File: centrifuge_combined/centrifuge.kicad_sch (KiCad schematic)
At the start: 4 parts, among them J504 Conn_02x05_Odd_Even, J518 Conn_02x03_Odd_Even, J519 Conn_02x02_Odd_Even

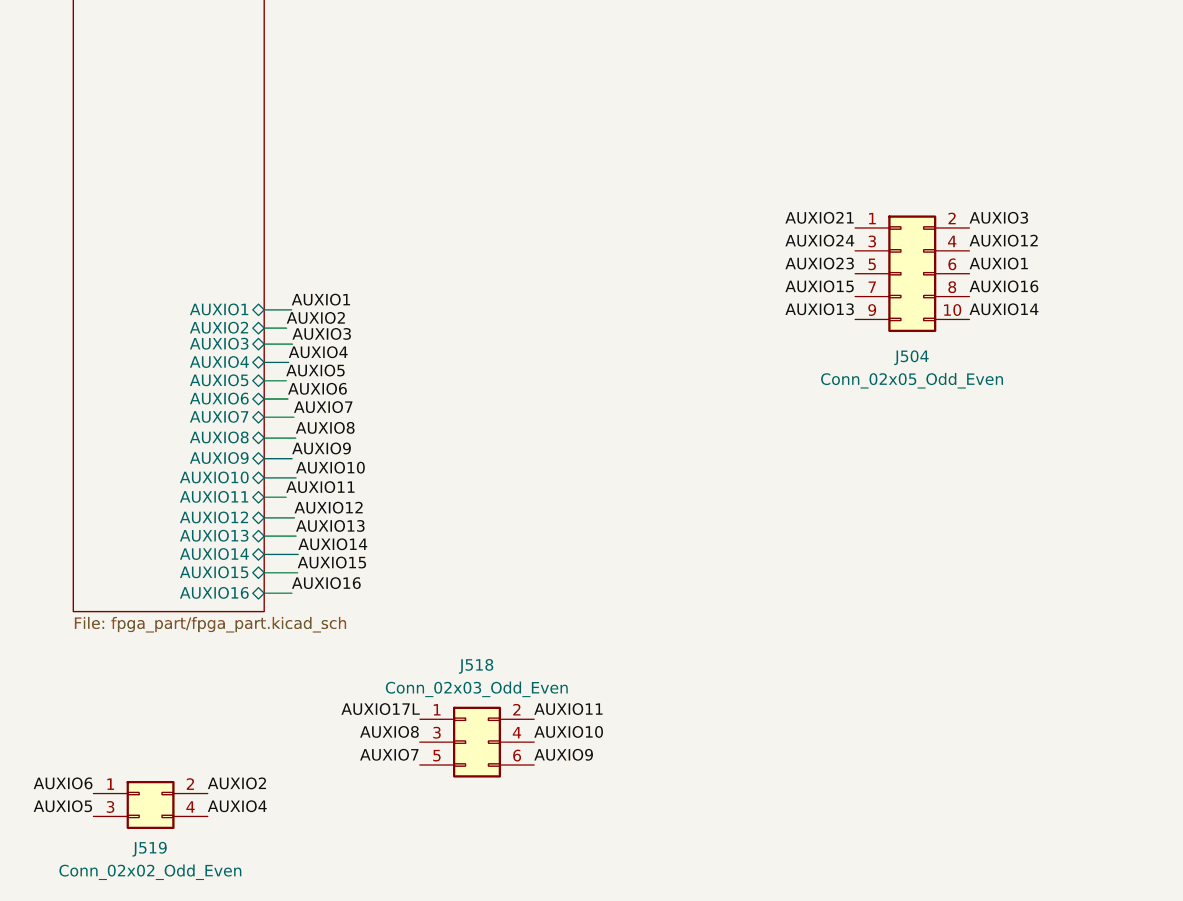
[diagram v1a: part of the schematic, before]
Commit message: more checks, also make silkscreen text for connectors
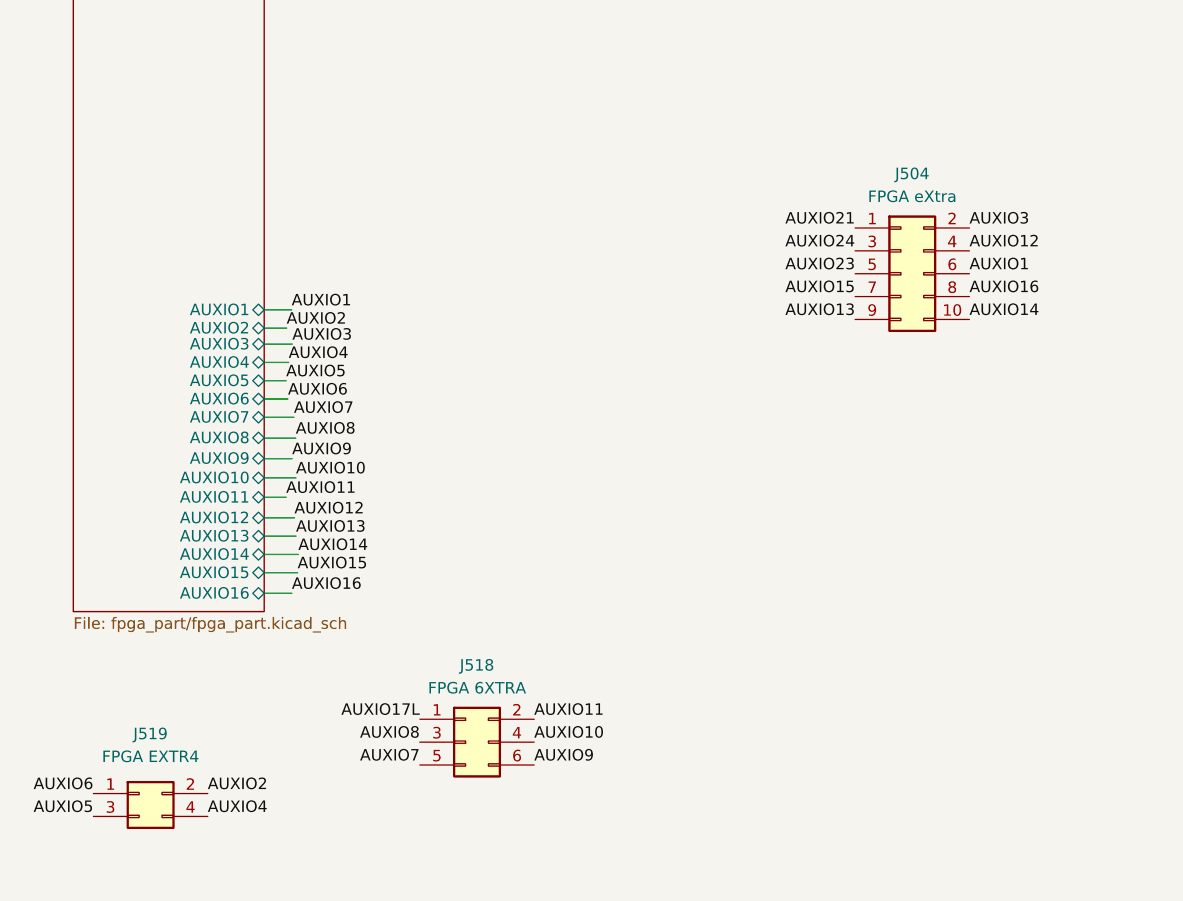
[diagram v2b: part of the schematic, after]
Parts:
- J504: value Conn_02x05_Odd_Even -> FPGA eXtra
- J518: value Conn_02x03_Odd_Even -> FPGA 6XTRA
- J519: value Conn_02x02_Odd_Even -> FPGA EXTR4
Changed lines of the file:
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@@
     (in_bom yes) (on_board yes) (fields_autoplaced)
     (property "Reference" "J518" (id 0) (at 114.1984 172.72 0))
-    (property "Value" "Conn_02x03_Odd_Even" (id 1) (at 114.1984 175.26 0))
+    (property "Value" "FPGA 6XTRA" (id 1) (at 114.1984 175.26 0))
     (property "Footprint" "Connector_PinHeader_2.54mm:PinHeader_2x03_P2.54mm_Vertical" (id 2) (at 112.9284 181.2544 0)
       (effects (font (size 1.27 1.27)) hide)
@@
   (symbol (lib_id "Connector_Generic:Conn_02x02_Odd_Even") (at 76.6572 186.9694 0) (unit 1)
     (in_bom yes) (on_board yes) (fields_autoplaced)
-    (property "Reference" "J519" (id 0) (at 77.9272 193.04 0))
-    (property "Value" "Conn_02x02_Odd_Even" (id 1) (at 77.9272 195.58 0))
+    (property "Reference" "J519" (id 0) (at 77.9272 180.34 0))
+    (property "Value" "FPGA EXTR4" (id 1) (at 77.9272 182.88 0))
     (property "Footprint" "Connector_PinHeader_2.54mm:PinHeader_2x02_P2.54mm_Vertical" (id 2) (at 76.6572 186.9694 0)
       (effects (font (size 1.27 1.27)) hide)
@@
   (symbol (lib_id "Connector_Generic:Conn_02x05_Odd_Even") (at 161.29 129.2098 0) (unit 1)
     (in_bom yes) (on_board yes) (fields_autoplaced)
-    (property "Reference" "J504" (id 0) (at 162.56 138.43 0))
-    (property "Value" "Conn_02x05_Odd_Even" (id 1) (at 162.56 140.97 0))
+    (property "Reference" "J504" (id 0) (at 162.56 118.11 0))
+    (property "Value" "FPGA eXtra" (id 1) (at 162.56 120.65 0))
     (property "Footprint" "Connector_PinHeader_2.54mm:PinHeader_2x05_P2.54mm_Vertical" (id 2) (at 161.29 129.2098 0)
       (effects (font (size 1.27 1.27)) hide)
@@
       (reference "#PWR0122") (unit 1) (value "+5V") (footprint "")
     )
+    (path "/e1575795-d3d5-4c3d-a0f9-e66719ec181c/98fec552-a155-4b2e-a0db-8f682b2e047b"
+      (reference "#PWR0123") (unit 1) (value "+3V3_FPGA") (footprint "")
+    )
     (path "/e1575795-d3d5-4c3d-a0f9-e66719ec181c/9c253e80-2b56-46fb-bbe0-8c25e23a6733/cee8dd18-ae90-4ef7-82e5-f924274ba04a"
       (reference "#PWR0124") (unit 1) (value "+3V3") (footprint "")
@@
       (reference "#PWR0189") (unit 1) (value "+5V_FPGA") (footprint "")
     )
+    (path "/e1575795-d3d5-4c3d-a0f9-e66719ec181c/f1e8b8ff-8293-4a66-bf3d-2505ef83bc55"
+      (reference "#PWR0190") (unit 1) (value "+3V3_FPGA") (footprint "")
+    )
     (path "/e1575795-d3d5-4c3d-a0f9-e66719ec181c/41448e64-f8a6-4898-94db-9af1b3d7cee9/dd33a722-3105-430e-ae1f-18734fe91dc7"
       (reference "#PWR0191") (unit 1) (value "GND") (footprint "")
@@
       (reference "#PWR0539") (unit 1) (value "GND") (footprint "")
     )
-    (path "/e1575795-d3d5-4c3d-a0f9-e66719ec181c/98fec552-a155-4b2e-a0db-8f682b2e047b"
-      (reference "#PWR?") (unit 1) (value "+3V3_FPGA") (footprint "")
-    )
-    (path "/e1575795-d3d5-4c3d-a0f9-e66719ec181c/f1e8b8ff-8293-4a66-bf3d-2505ef83bc55"
-      (reference "#PWR?") (unit 1) (value "+3V3_FPGA") (footprint "")
-    )
     (path "/e1575795-d3d5-4c3d-a0f9-e66719ec181c/634c7769-4266-4d3f-b715-4b9767b6d9de/90142074-d6ae-4f09-8dd2-e143c0d83720"
       (reference "C1") (unit 1) (value "10u") (footprint "Capacitor_SMD:C_0805_2012Metric_Pad1.18x1.45mm_HandSolder")
@@
     )
     (path "/e1575795-d3d5-4c3d-a0f9-e66719ec181c/dc0aff80-49aa-4f2d-b505-209791422e22/9bb45a87-ba44-4f62-9b71-001a5d1cfb78"
-      (reference "J1") (unit 1) (value "Conn_02x07_Odd_Even") (footprint "centrifuge footprints:878311411")
+      (reference "J1") (unit 1) (value "FPGA JTAG") (footprint "centrifuge footprints:878311411")
     )
     (path "/e1575795-d3d5-4c3d-a0f9-e66719ec181c/9c253e80-2b56-46fb-bbe0-8c25e23a6733/c50ed301-9691-45b4-8160-e577727037b4"
@@
     )
     (path "/e1c91b2f-9f46-43e0-9803-4154ea32a4bf"
-      (reference "J504") (unit 1) (value "Conn_02x05_Odd_Even") (footprint "Connector_PinHeader_2.54mm:PinHeader_2x05_P2.54mm_Vertical")
+      (reference "J504") (unit 1) (value "FPGA eXtra") (footprint "Connector_PinHeader_2.54mm:PinHeader_2x05_P2.54mm_Vertical")
     )
     (path "/02dc33a2-ea39-47d9-957e-80e0f80f4644/12449800-d3ac-47fd-8345-77581e9ee736"
@@
     )
     (path "/065c7614-f1e5-43f4-9e51-37aa46a50f51"
-      (reference "J518") (unit 1) (value "Conn_02x03_Odd_Even") (footprint "Connector_PinHeader_2.54mm:PinHeader_2x03_P2.54mm_Vertical")
+      (reference "J518") (unit 1) (value "FPGA 6XTRA") (footprint "Connector_PinHeader_2.54mm:PinHeader_2x03_P2.54mm_Vertical")
     )
     (path "/9b781762-538b-48b9-8478-fa6a861b4795"
-      (reference "J519") (unit 1) (value "Conn_02x02_Odd_Even") (footprint "Connector_PinHeader_2.54mm:PinHeader_2x02_P2.54mm_Vertical")
+      (reference "J519") (unit 1) (value "FPGA EXTR4") (footprint "Connector_PinHeader_2.54mm:PinHeader_2x02_P2.54mm_Vertical")
     )
     (path "/e1575795-d3d5-4c3d-a0f9-e66719ec181c/9c253e80-2b56-46fb-bbe0-8c25e23a6733/5b9b0cf7-ae06-48c3-84da-0cf76e29bfc8"

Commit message: Fixed Elprint complaints and JTAG VREF problems+config flash CS
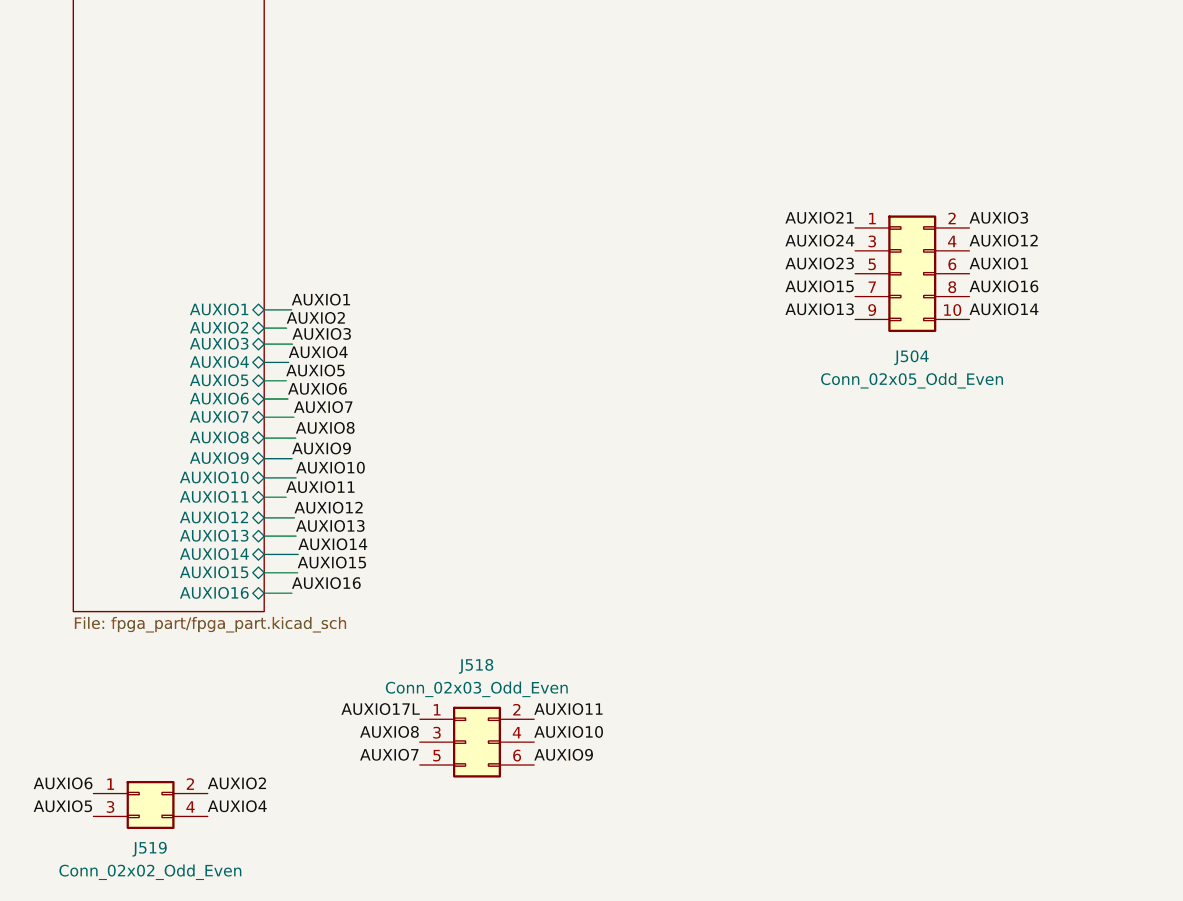
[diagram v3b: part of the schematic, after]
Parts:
- J504: value FPGA eXtra -> Conn_02x05_Odd_Even
- J518: value FPGA 6XTRA -> Conn_02x03_Odd_Even
- J519: value FPGA EXTR4 -> Conn_02x02_Odd_Even
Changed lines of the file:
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@@
   (title_block
     (title "VGA Centrifuge")
-    (date "2022-10-03")
-    (rev "R3")
+    (date "2022-10-05")
+    (rev "R4")
     (comment 1 "Author: Paolo Celati")
     (comment 2 "Toplevel")
@@
     (in_bom yes) (on_board yes) (fields_autoplaced)
     (property "Reference" "J518" (id 0) (at 114.1984 172.72 0))
-    (property "Value" "FPGA 6XTRA" (id 1) (at 114.1984 175.26 0))
+    (property "Value" "Conn_02x03_Odd_Even" (id 1) (at 114.1984 175.26 0))
     (property "Footprint" "Connector_PinHeader_2.54mm:PinHeader_2x03_P2.54mm_Vertical" (id 2) (at 112.9284 181.2544 0)
       (effects (font (size 1.27 1.27)) hide)
@@
   (symbol (lib_id "Connector_Generic:Conn_02x02_Odd_Even") (at 76.6572 186.9694 0) (unit 1)
     (in_bom yes) (on_board yes) (fields_autoplaced)
-    (property "Reference" "J519" (id 0) (at 77.9272 180.34 0))
-    (property "Value" "FPGA EXTR4" (id 1) (at 77.9272 182.88 0))
+    (property "Reference" "J519" (id 0) (at 77.9272 193.04 0))
+    (property "Value" "Conn_02x02_Odd_Even" (id 1) (at 77.9272 195.58 0))
     (property "Footprint" "Connector_PinHeader_2.54mm:PinHeader_2x02_P2.54mm_Vertical" (id 2) (at 76.6572 186.9694 0)
       (effects (font (size 1.27 1.27)) hide)
@@
   (symbol (lib_id "Connector_Generic:Conn_02x05_Odd_Even") (at 161.29 129.2098 0) (unit 1)
     (in_bom yes) (on_board yes) (fields_autoplaced)
-    (property "Reference" "J504" (id 0) (at 162.56 118.11 0))
-    (property "Value" "FPGA eXtra" (id 1) (at 162.56 120.65 0))
+    (property "Reference" "J504" (id 0) (at 162.56 138.43 0))
+    (property "Value" "Conn_02x05_Odd_Even" (id 1) (at 162.56 140.97 0))
     (property "Footprint" "Connector_PinHeader_2.54mm:PinHeader_2x05_P2.54mm_Vertical" (id 2) (at 161.29 129.2098 0)
       (effects (font (size 1.27 1.27)) hide)
@@
       (reference "#PWR0122") (unit 1) (value "+5V") (footprint "")
     )
-    (path "/e1575795-d3d5-4c3d-a0f9-e66719ec181c/98fec552-a155-4b2e-a0db-8f682b2e047b"
-      (reference "#PWR0123") (unit 1) (value "+3V3_FPGA") (footprint "")
+    (path "/e1575795-d3d5-4c3d-a0f9-e66719ec181c/9c253e80-2b56-46fb-bbe0-8c25e23a6733/85738c56-05dd-4498-92d7-f3e46fbd4d59"
+      (reference "#PWR0123") (unit 1) (value "+1V8") (footprint "")
     )
     (path "/e1575795-d3d5-4c3d-a0f9-e66719ec181c/9c253e80-2b56-46fb-bbe0-8c25e23a6733/cee8dd18-ae90-4ef7-82e5-f924274ba04a"
@@
       (reference "#PWR0176") (unit 1) (value "+5V") (footprint "")
     )
-    (path "/e1575795-d3d5-4c3d-a0f9-e66719ec181c/e67fdb3f-7e85-477f-8134-0287c1754cef"
-      (reference "#PWR0177") (unit 1) (value "+1V8_FPGA") (footprint "")
+    (path "/e1575795-d3d5-4c3d-a0f9-e66719ec181c/3e4fbc07-93ba-4c68-9b2c-ce8f536b353e/85738c56-05dd-4498-92d7-f3e46fbd4d59"
+      (reference "#PWR0177") (unit 1) (value "+1V8") (footprint "")
     )
     (path "/e1575795-d3d5-4c3d-a0f9-e66719ec181c/3e4fbc07-93ba-4c68-9b2c-ce8f536b353e/dd33a722-3105-430e-ae1f-18734fe91dc7"
@@
       (reference "#PWR0189") (unit 1) (value "+5V_FPGA") (footprint "")
     )
-    (path "/e1575795-d3d5-4c3d-a0f9-e66719ec181c/f1e8b8ff-8293-4a66-bf3d-2505ef83bc55"
-      (reference "#PWR0190") (unit 1) (value "+3V3_FPGA") (footprint "")
+    (path "/e1575795-d3d5-4c3d-a0f9-e66719ec181c/41448e64-f8a6-4898-94db-9af1b3d7cee9/85738c56-05dd-4498-92d7-f3e46fbd4d59"
+      (reference "#PWR0190") (unit 1) (value "+1V8_FPGA") (footprint "")
     )
     (path "/e1575795-d3d5-4c3d-a0f9-e66719ec181c/41448e64-f8a6-4898-94db-9af1b3d7cee9/dd33a722-3105-430e-ae1f-18734fe91dc7"
@@
       (reference "#PWR0221") (unit 1) (value "GND") (footprint "")
     )
+    (path "/e1575795-d3d5-4c3d-a0f9-e66719ec181c/4c7a3b57-3605-49ef-8431-d3fca3e33250/0c8c7057-0ebc-4afa-b245-78462fd8816a"
+      (reference "#PWR0222") (unit 1) (value "+3V3_FPGA") (footprint "")
+    )
     (path "/e1575795-d3d5-4c3d-a0f9-e66719ec181c/dc0aff80-49aa-4f2d-b505-209791422e22/f663a6f9-0b20-4f6e-9953-88323eee8805"
       (reference "#PWR0223") (unit 1) (value "+3V3_FPGA") (footprint "")
@@
     )
     (path "/e1575795-d3d5-4c3d-a0f9-e66719ec181c/dc0aff80-49aa-4f2d-b505-209791422e22/9bb45a87-ba44-4f62-9b71-001a5d1cfb78"
-      (reference "J1") (unit 1) (value "FPGA JTAG") (footprint "centrifuge footprints:878311411")
+      (reference "J1") (unit 1) (value "Conn_02x07_Odd_Even") (footprint "centrifuge footprints:878311411")
     )
     (path "/e1575795-d3d5-4c3d-a0f9-e66719ec181c/9c253e80-2b56-46fb-bbe0-8c25e23a6733/c50ed301-9691-45b4-8160-e577727037b4"
@@
     )
     (path "/02dc33a2-ea39-47d9-957e-80e0f80f4644/64ddcf41-2be8-44c4-9b4f-c144dbd415f7"
-      (reference "J503") (unit 1) (value "MCU_extra") (footprint "Connector_PinHeader_2.54mm:PinHeader_1x04_P2.54mm_Vertical")
+      (reference "J503") (unit 1) (value "FPGA_extra") (footprint "Connector_PinHeader_2.54mm:PinHeader_1x04_P2.54mm_Vertical")
     )
     (path "/e1c91b2f-9f46-43e0-9803-4154ea32a4bf"
-      (reference "J504") (unit 1) (value "FPGA eXtra") (footprint "Connector_PinHeader_2.54mm:PinHeader_2x05_P2.54mm_Vertical")
+      (reference "J504") (unit 1) (value "Conn_02x05_Odd_Even") (footprint "Connector_PinHeader_2.54mm:PinHeader_2x05_P2.54mm_Vertical")
     )
     (path "/02dc33a2-ea39-47d9-957e-80e0f80f4644/12449800-d3ac-47fd-8345-77581e9ee736"
@@
     )
     (path "/065c7614-f1e5-43f4-9e51-37aa46a50f51"
-      (reference "J518") (unit 1) (value "FPGA 6XTRA") (footprint "Connector_PinHeader_2.54mm:PinHeader_2x03_P2.54mm_Vertical")
+      (reference "J518") (unit 1) (value "Conn_02x03_Odd_Even") (footprint "Connector_PinHeader_2.54mm:PinHeader_2x03_P2.54mm_Vertical")
     )
     (path "/9b781762-538b-48b9-8478-fa6a861b4795"
-      (reference "J519") (unit 1) (value "FPGA EXTR4") (footprint "Connector_PinHeader_2.54mm:PinHeader_2x02_P2.54mm_Vertical")
+      (reference "J519") (unit 1) (value "Conn_02x02_Odd_Even") (footprint "Connector_PinHeader_2.54mm:PinHeader_2x02_P2.54mm_Vertical")
     )
     (path "/e1575795-d3d5-4c3d-a0f9-e66719ec181c/9c253e80-2b56-46fb-bbe0-8c25e23a6733/5b9b0cf7-ae06-48c3-84da-0cf76e29bfc8"
@@
       (reference "R54") (unit 1) (value "330") (footprint "Resistor_SMD:R_0805_2012Metric_Pad1.20x1.40mm_HandSolder")
     )
+    (path "/e1575795-d3d5-4c3d-a0f9-e66719ec181c/4c7a3b57-3605-49ef-8431-d3fca3e33250/1c25aaff-795a-4c7a-a448-27d59a695932"
+      (reference "R55") (unit 1) (value "2.2k") (footprint "Resistor_SMD:R_0805_2012Metric_Pad1.20x1.40mm_HandSolder")
+    )
     (path "/02dc33a2-ea39-47d9-957e-80e0f80f4644/fbdfdf53-0af0-4881-86b7-bda43037c5c0"
       (reference "R501") (unit 1) (value "2.2k") (footprint "Resistor_SMD:R_0805_2012Metric_Pad1.20x1.40mm_HandSolder")
@@
     )
     (path "/e1575795-d3d5-4c3d-a0f9-e66719ec181c/634c7769-4266-4d3f-b715-4b9767b6d9de/6910358c-e92c-45c1-a24a-80dfc23ba030"
-      (reference "U5") (unit 1) (value "THS8136") (footprint "Package_QFP:LQFP-48-1EP_7x7mm_P0.5mm_EP3.6x3.6mm")
+      (reference "U5") (unit 1) (value "THS8136") (footprint "centrifuge footprints:LQFP-48-1EP_7x7mm_P0.5mm_EP3.6x3.6mm_ThermalVias_modified")
     )
     (path "/e1575795-d3d5-4c3d-a0f9-e66719ec181c/9c253e80-2b56-46fb-bbe0-8c25e23a6733/f40b1711-a16a-4dcd-9870-5df08d87996b"
